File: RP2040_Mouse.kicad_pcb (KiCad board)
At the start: 2 copper layers, 54.6 x 30.8 mm, 43 parts, among them J1 DB9_Male, J2 Barrel_Jack_Switch, J3 USB_A, Q1 Q_NPN_BEC, SW1 SW_DPDT_x2, U1 LSF0108PWR, U2 RP2040, U3 AT25SF081B-SSHD-T, U4 AMS1117-3.3, Y1 12MHZ

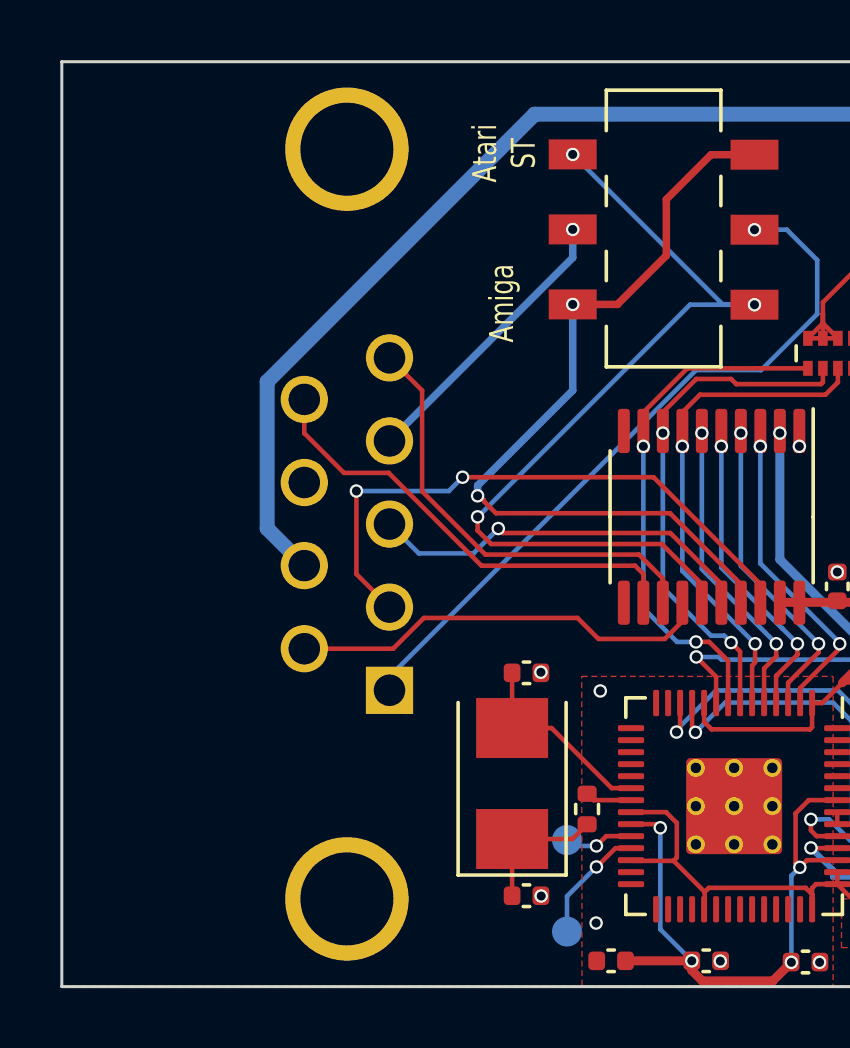
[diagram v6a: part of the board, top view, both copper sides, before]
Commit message: Break up schematic into hierarchical sheets
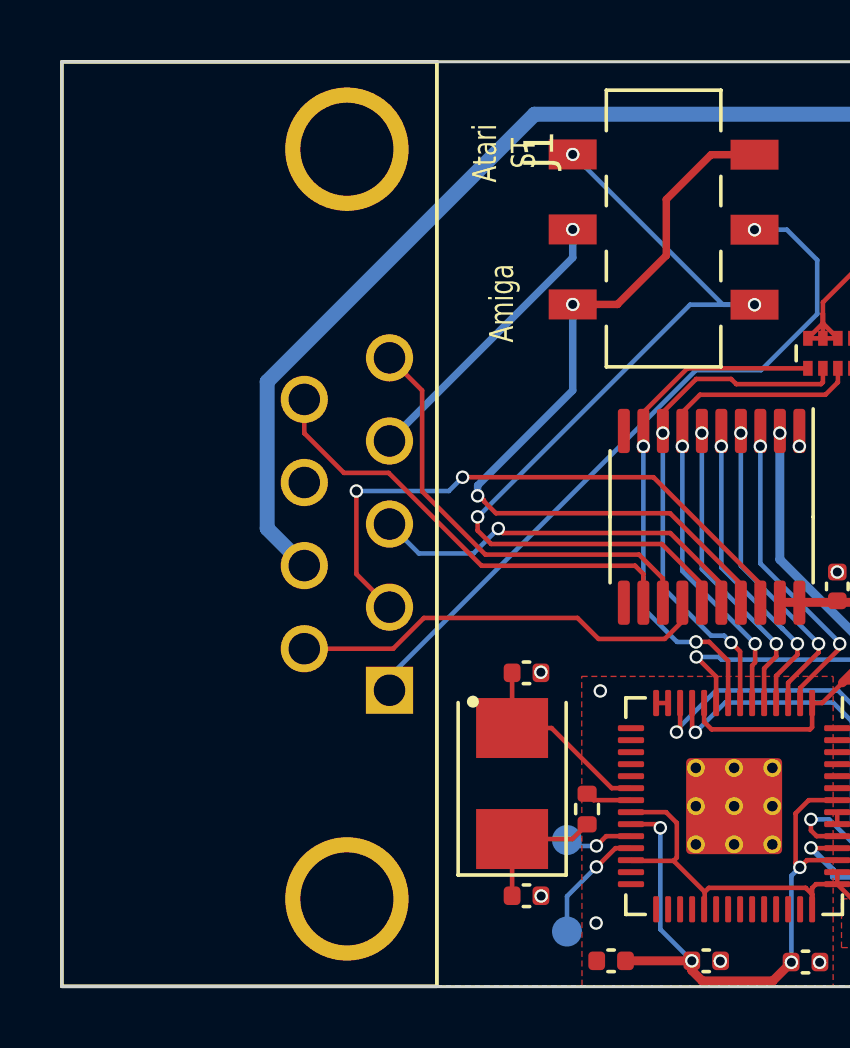
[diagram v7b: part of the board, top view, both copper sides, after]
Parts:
- G***: footprint My Libs:dl_logo_small -> My Library:dl_logo_small
- J1: footprint SmallyMouse QFN64-backups:ASSMANN_A-DF_09_A_KG-T2S -> My Library:ASSMANN_A-DF_09_A_KG-T2S
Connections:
- net /LSF0108_VREFB_EN renamed /Logic Level Shift/LSF0108_VREFB_EN
- net /M_LED renamed /Indication/M_LED
- net /M_LED_L renamed /Indication/M_LED_L
- net /P_LED_L renamed /Indication/P_LED_L
- net /SWCLK renamed /Microcontroller/SWCLK
- net /SWD renamed /Microcontroller/SWD
- net /USB_T_D+ renamed /Microcontroller/USB_T_D+
- net /USB_T_D- renamed /Microcontroller/USB_T_D-
- net /XIN renamed /Microcontroller/XIN
- net /XOUT renamed /Microcontroller/XOUT
- net /XOUT_LTD renamed /Microcontroller/XOUT_LTD
- net /~{USB_BOOT} renamed /Microcontroller/~{USB_BOOT}

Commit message: Rev 5 update
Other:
- board text added: "5v MAX 400ma"
- board text removed: "9v MAX 400ma"
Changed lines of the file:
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@@
   (title_block
     (title "RP2040 USB to Quadrature Mouse Adaptor")
-    (date "2023-01-21")
-    (rev "5")
+    (date "2023-02-03")
+    (rev "6")
     (company "Darren's Lab")
   )
@@
       (drillshape 0)
       (scaleselection 1)
-      (outputdirectory "gerbers")
+      (outputdirectory "gerbers_pcbway/")
     )
   )
@@
     (fp_line (start 3.5 3.5) (end -3.5 3.5)
       (stroke (width 0.1) (type solid)) (layer "F.Fab"))
-    (pad "" smd roundrect (at -0.6375 -0.6375 270) (size 1.084435 1.084435) (layers "F.Paste") (roundrect_rratio 0.230535))
-    (pad "" smd roundrect (at -0.6375 0.6375 270) (size 1.084435 1.084435) (layers "F.Paste") (roundrect_rratio 0.230535))
-    (pad "" smd roundrect (at 0.6375 -0.6375 270) (size 1.084435 1.084435) (layers "F.Paste") (roundrect_rratio 0.230535))
-    (pad "" smd roundrect (at 0.6375 0.6375 270) (size 1.084435 1.084435) (layers "F.Paste") (roundrect_rratio 0.230535))
+    (pad "" smd roundrect (at -0.6375 -0.6375 270) (size 1.084435 1.084435) (layers "F.Paste") (roundrect_rratio 0.2305347946))
+    (pad "" smd roundrect (at -0.6375 0.6375 270) (size 1.084435 1.084435) (layers "F.Paste") (roundrect_rratio 0.2305347946))
+    (pad "" smd roundrect (at 0.6375 -0.6375 270) (size 1.084435 1.084435) (layers "F.Paste") (roundrect_rratio 0.2305347946))
+    (pad "" smd roundrect (at 0.6375 0.6375 270) (size 1.084435 1.084435) (layers "F.Paste") (roundrect_rratio 0.2305347946))
     (pad "1" smd roundrect (at -3.4375 -2.6 270) (size 0.875 0.2) (layers "F.Cu" "F.Paste" "F.Mask") (roundrect_rratio 0.25)
       (net 3 "+3V3") (pinfunction "IOVDD") (pintype "power_in"))
@@
     (effects (font (size 0.8 0.6) (thickness 0.15)) (justify mirror))
   )
-  (gr_text "9v MAX\n400ma" (at 170.798912 98.860526 90) (layer "B.SilkS")
+  (gr_text "5v MAX\n400ma" (at 170.798912 98.860526 90) (layer "B.SilkS")
     (effects (font (size 0.8 0.6) (thickness 0.15)) (justify mirror))
   )
